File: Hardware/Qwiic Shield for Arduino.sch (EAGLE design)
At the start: 35 parts, among them Q1 200mA/50V, Q2 200mA/50V, U1 ARDUINO UNO

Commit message: Adding mounting spot for Qwiic boards
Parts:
- removed J11, J12, J13, J14, J15, J16, J17, J18, J19, J20, J21, J22, J5, J7: (no value), SparkX:CONN_18NO_SILK
- added U$3: QWIIC_BOARD_OUTLINEH, SparkX:QWIIC_BOARD_OUTLINEH
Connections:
- removed net N$1: J5.2, J7.2
- removed net N$10: J5.11, J7.11
- removed net N$100: J19.11, J20.11
- removed net N$101: J19.12, J20.12
- removed net N$102: J19.13, J20.13
- removed net N$103: J19.14, J20.14
- removed net N$104: J19.15, J20.15
- removed net N$105: J19.16, J20.16
- removed net N$106: J19.17, J20.17
- removed net N$107: J19.18, J20.18
- removed net N$108: J19.1, J20.1
- removed net N$109: J21.2, J22.2
- removed net N$11: J5.12, J7.12
- removed net N$110: J21.3, J22.3
- removed net N$111: J21.4, J22.4
- removed net N$112: J21.5, J22.5
- removed net N$113: J21.6, J22.6
- removed net N$114: J21.7, J22.7
- removed net N$115: J21.8, J22.8
- removed net N$116: J21.9, J22.9
- removed net N$117: J21.10, J22.10
- removed net N$118: J21.11, J22.11
- removed net N$119: J21.12, J22.12
- removed net N$12: J5.13, J7.13
- removed net N$120: J21.13, J22.13
- removed net N$121: J21.14, J22.14
- removed net N$122: J21.15, J22.15
- removed net N$123: J21.16, J22.16
- removed net N$124: J21.17, J22.17
- removed net N$125: J21.18, J22.18
- removed net N$126: J21.1, J22.1
- removed net N$13: J5.14, J7.14
- removed net N$14: J5.15, J7.15
- removed net N$15: J5.16, J7.16
- removed net N$16: J5.17, J7.17
- removed net N$17: J5.18, J7.18
- removed net N$18: J5.1, J7.1
- removed net N$19: J13.2, J14.2
- removed net N$2: J5.3, J7.3
- removed net N$20: J13.3, J14.3
- removed net N$21: J11.2, J12.2
- removed net N$22: J11.3, J12.3
- removed net N$23: J11.4, J12.4
- removed net N$24: J11.5, J12.5
- removed net N$25: J11.6, J12.6
- removed net N$26: J11.7, J12.7
- removed net N$27: J11.8, J12.8
- removed net N$28: J11.9, J12.9
- removed net N$29: J11.10, J12.10
- removed net N$3: J5.4, J7.4
- removed net N$30: J11.11, J12.11
- removed net N$31: J11.12, J12.12
- removed net N$32: J11.13, J12.13
- removed net N$33: J11.14, J12.14
- removed net N$34: J11.15, J12.15
- removed net N$35: J11.16, J12.16
- removed net N$36: J11.17, J12.17
- removed net N$37: J11.18, J12.18
- removed net N$38: J11.1, J12.1
- removed net N$39: J13.4, J14.4
- removed net N$4: J5.5, J7.5
- removed net N$40: J13.5, J14.5
- removed net N$41: J13.6, J14.6
- removed net N$42: J13.7, J14.7
- removed net N$43: J13.8, J14.8
- removed net N$44: J13.9, J14.9
- removed net N$45: J13.10, J14.10
- removed net N$46: J13.11, J14.11
- removed net N$47: J13.12, J14.12
- removed net N$48: J13.13, J14.13
- removed net N$49: J13.14, J14.14
- removed net N$5: J5.6, J7.6
- removed net N$50: J13.15, J14.15
- removed net N$51: J13.16, J14.16
- removed net N$52: J13.17, J14.17
- removed net N$53: J13.18, J14.18
- removed net N$54: J13.1, J14.1
- removed net N$55: J15.2, J16.2
- removed net N$56: J15.3, J16.3
- removed net N$57: J15.4, J16.4
- removed net N$58: J15.5, J16.5
- removed net N$59: J15.6, J16.6
- removed net N$6: J5.7, J7.7
- removed net N$60: J15.7, J16.7
- removed net N$61: J15.8, J16.8
- removed net N$62: J15.9, J16.9
- removed net N$63: J15.10, J16.10
- removed net N$64: J15.11, J16.11
- removed net N$65: J15.12, J16.12
- removed net N$66: J15.13, J16.13
- removed net N$67: J15.14, J16.14
- removed net N$68: J15.15, J16.15
- removed net N$69: J15.16, J16.16
- removed net N$7: J5.8, J7.8
- removed net N$70: J15.17, J16.17
- removed net N$71: J15.18, J16.18
- removed net N$72: J15.1, J16.1
- removed net N$73: J17.2, J18.2
- removed net N$74: J17.3, J18.3
- removed net N$75: J17.4, J18.4
- removed net N$76: J17.5, J18.5
- removed net N$77: J17.6, J18.6
- removed net N$78: J17.7, J18.7
- removed net N$79: J17.8, J18.8
- removed net N$8: J5.9, J7.9
- removed net N$80: J17.9, J18.9
- removed net N$81: J17.10, J18.10
- removed net N$82: J17.11, J18.11
- removed net N$83: J17.12, J18.12
- removed net N$84: J17.13, J18.13
- removed net N$85: J17.14, J18.14
- removed net N$86: J17.15, J18.15
- removed net N$87: J17.16, J18.16
- removed net N$88: J17.17, J18.17
- removed net N$89: J17.18, J18.18
- removed net N$9: J5.10, J7.10
- removed net N$90: J17.1, J18.1
- removed net N$91: J19.2, J20.2
- removed net N$92: J19.3, J20.3
- removed net N$93: J19.4, J20.4
- removed net N$94: J19.5, J20.5
- removed net N$95: J19.6, J20.6
- removed net N$96: J19.7, J20.7
- removed net N$97: J19.8, J20.8
- removed net N$98: J19.9, J20.9
- removed net N$99: J19.10, J20.10
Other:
- note removed: "Prototyping Connections"
- moved on the sheet: J2, J3, J4, J6, Q1, Q2, R2, R3, R4, R5, U1

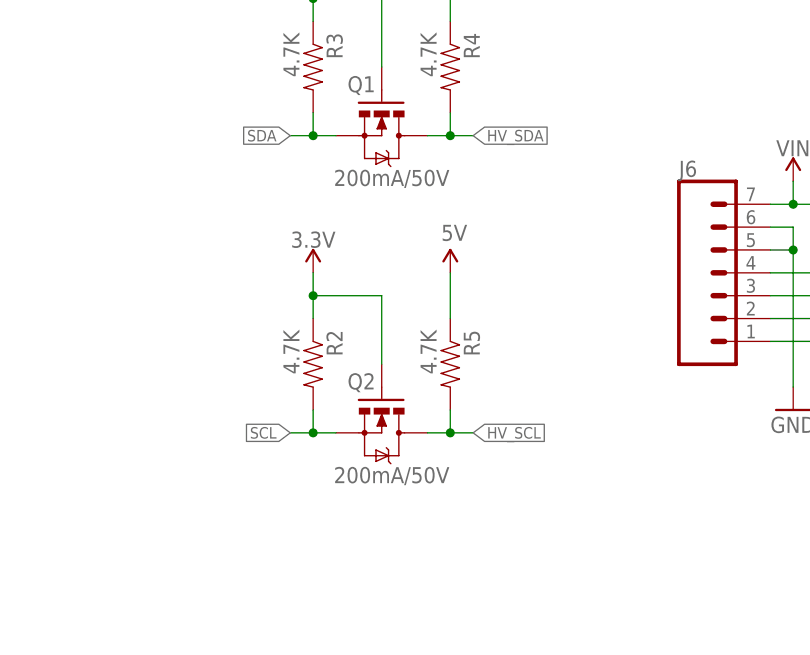
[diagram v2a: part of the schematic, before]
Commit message: Adding Qwiic mounting holes to shield
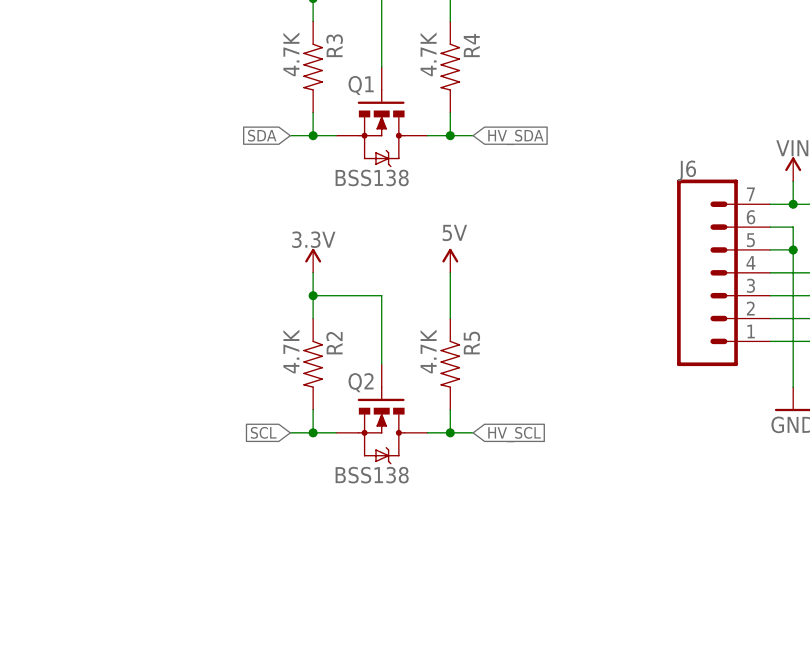
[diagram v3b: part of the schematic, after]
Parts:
- Q1, Q2: value 200mA/50V -> BSS138
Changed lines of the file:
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@@
 <part name="FRAME1" library="SparkFun-Aesthetics" deviceset="FRAME-LETTER" device=""/>
 <part name="GND1" library="SparkFun" deviceset="GND" device=""/>
-<part name="Q1" library="SparkFun-DiscreteSemi" deviceset="MOSFET-NCHANNEL" device="BSS138" value="200mA/50V"/>
+<part name="Q1" library="SparkFun-DiscreteSemi" deviceset="MOSFET-NCHANNEL" device="BSS138" value="BSS138"/>
 <part name="R3" library="SparkFun-Resistors" deviceset="4.7KOHM-1/10W-1%(0603)" device="" value="4.7K"/>
 <part name="R4" library="SparkFun-Resistors" deviceset="4.7KOHM-1/10W-1%(0603)" device="" value="4.7K"/>
-<part name="Q2" library="SparkFun-DiscreteSemi" deviceset="MOSFET-NCHANNEL" device="BSS138" value="200mA/50V"/>
+<part name="Q2" library="SparkFun-DiscreteSemi" deviceset="MOSFET-NCHANNEL" device="BSS138" value="BSS138"/>
 <part name="R2" library="SparkFun-Resistors" deviceset="4.7KOHM-1/10W-1%(0603)" device="" value="4.7K"/>
 <part name="R5" library="SparkFun-Resistors" deviceset="4.7KOHM-1/10W-1%(0603)" device="" value="4.7K"/>
